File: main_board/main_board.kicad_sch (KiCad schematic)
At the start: 9 parts, among them J1 Bus_ISA_8bit, J2 IDE_44pin, J3 SIMM_30pin, J4 Keyboard, J5 Mouse, J6 5V_in, U1 M6117D, U2 SST39SF040

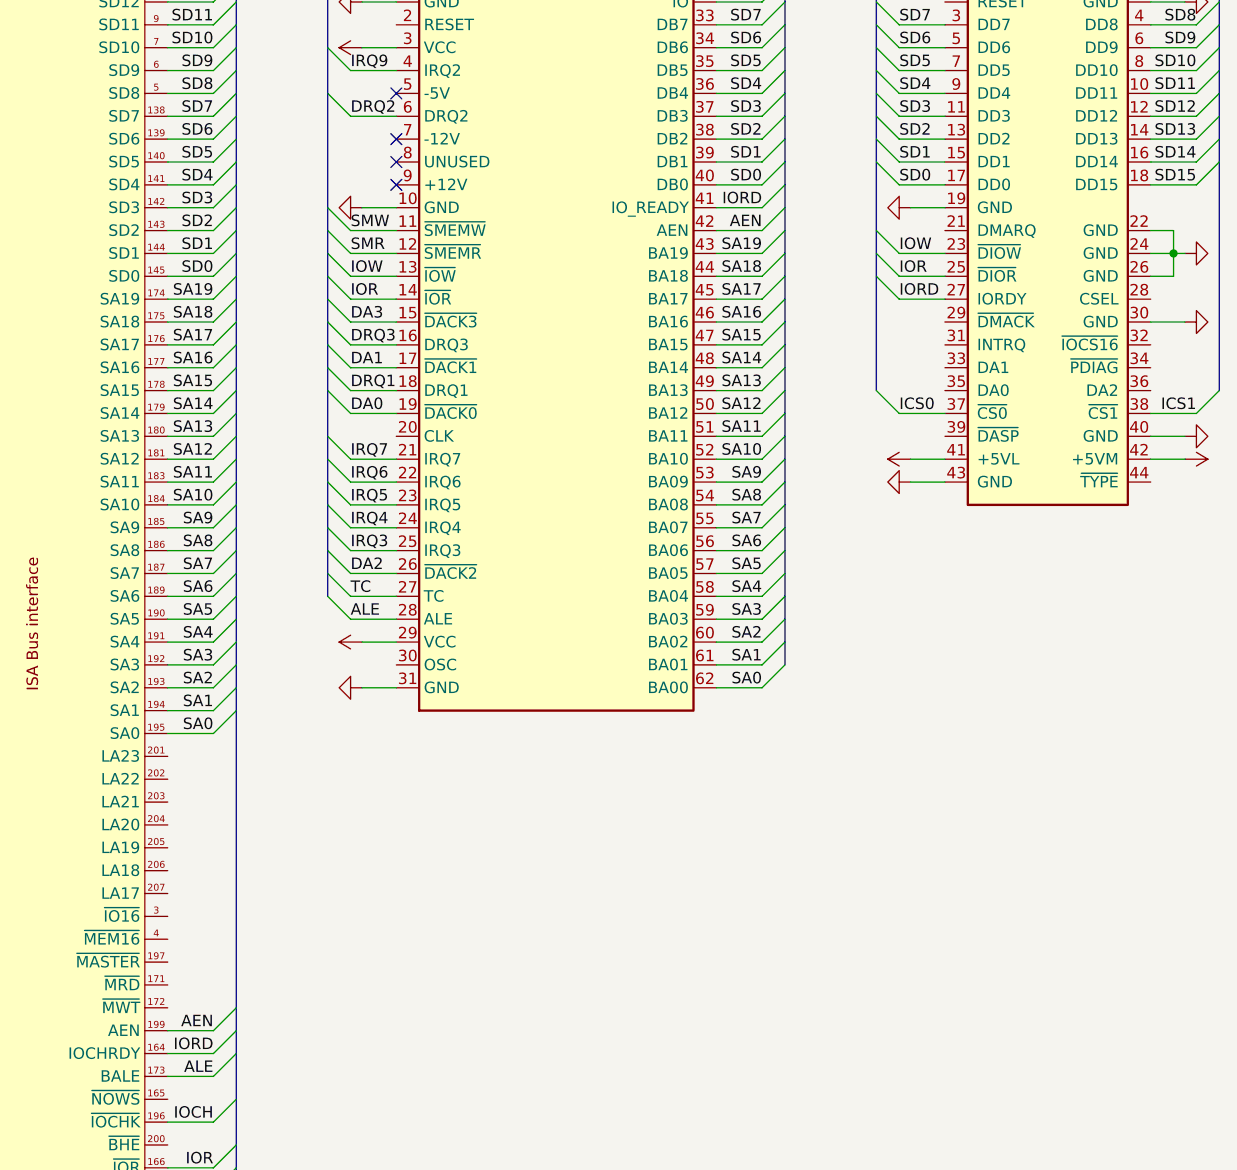
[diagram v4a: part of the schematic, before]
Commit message: connect IDE address lines to the bus
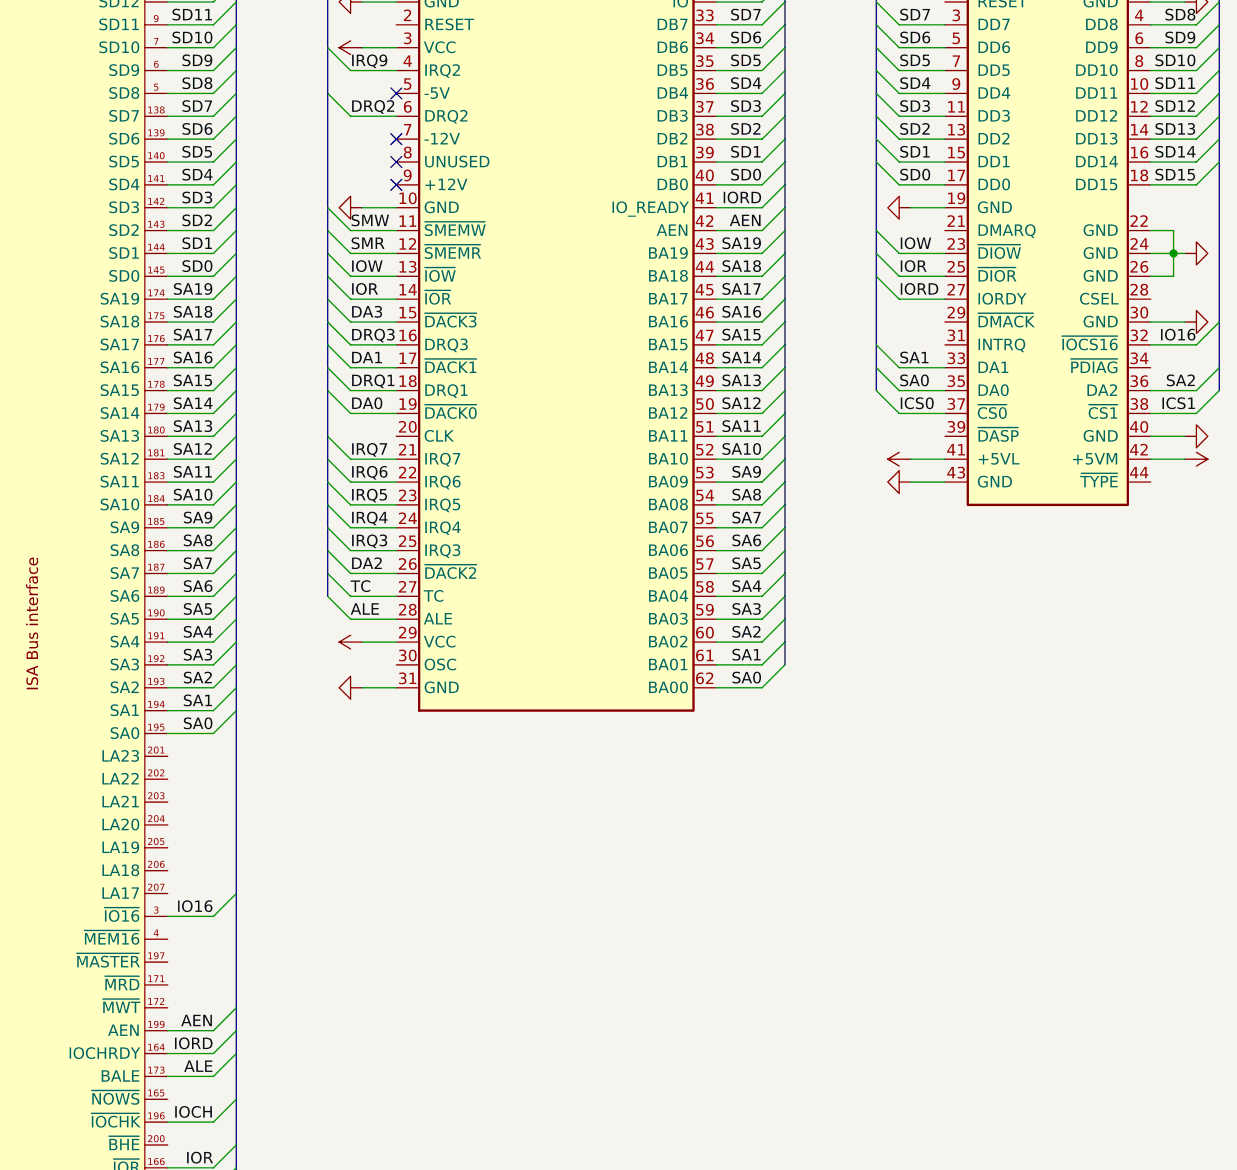
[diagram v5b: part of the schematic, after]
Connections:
- net SA0: now also J2.35 (DA0)
- net SA1: now also J2.33 (DA1)
- net SA2: now also J2.36 (DA2)
- net IO16: now reaches J2.32 (~{IOCS16})
- net IO16: now also U1.3 (~{IO16})
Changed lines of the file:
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@@
 	)
 	(bus_entry
+		(at 279.4 85.09)
+		(size 2.54 -2.54)
+		(stroke
+			(width 0)
+			(type default)
+		)
+	)
+	(bus_entry
 		(at 53.34 199.39)
 		(size 2.54 -2.54)
@@
 	)
 	(bus_entry
+		(at 246.38 90.17)
+		(size -2.54 -2.54)
+		(stroke
+			(width 0)
+			(type default)
+		)
+	)
+	(bus_entry
 		(at 53.34 250.19)
 		(size 2.54 -2.54)
@@
 	)
 	(bus_entry
+		(at 246.38 87.63)
+		(size -2.54 -2.54)
+		(stroke
+			(width 0)
+			(type default)
+		)
+	)
+	(bus_entry
 		(at 170.18 52.07)
 		(size 2.54 -2.54)
@@
 	)
 	(bus_entry
+		(at 279.4 90.17)
+		(size 2.54 -2.54)
+		(stroke
+			(width 0)
+			(type default)
+		)
+	)
+	(bus_entry
 		(at 170.18 87.63)
 		(size 2.54 -2.54)
@@
 	)
 	(bus_entry
+		(at 170.18 148.59)
+		(size 2.54 -2.54)
+		(stroke
+			(width 0)
+			(type default)
+		)
+	)
+	(bus_entry
 		(at 172.72 252.73)
 		(size -2.54 2.54)
@@
 	(bus
 		(pts
-			(xy 172.72 125.73) (xy 172.72 158.75)
+			(xy 172.72 125.73) (xy 172.72 146.05)
 		)
 		(stroke
@@
 		)
 	)
+	(bus
+		(pts
+			(xy 281.94 82.55) (xy 281.94 87.63)
+		)
+		(stroke
+			(width 0)
+			(type default)
+		)
+	)
 	(wire
 		(pts
@@
 	(wire
 		(pts
+			(xy 165.1 148.59) (xy 170.18 148.59)
+		)
+		(stroke
+			(width 0)
+			(type default)
+		)
+	)
+	(wire
+		(pts
 			(xy 165.1 57.15) (xy 170.18 57.15)
 		)
@@
 		)
 	)
+	(bus
+		(pts
+			(xy 243.84 85.09) (xy 243.84 77.47)
+		)
+		(stroke
+			(width 0)
+			(type default)
+		)
+	)
 	(wire
 		(pts
@@
 	(wire
 		(pts
+			(xy 274.32 85.09) (xy 279.4 85.09)
+		)
+		(stroke
+			(width 0)
+			(type default)
+		)
+	)
+	(wire
+		(pts
 			(xy 165.1 77.47) (xy 170.18 77.47)
 		)
@@
 		)
 	)
+	(bus
+		(pts
+			(xy 243.84 87.63) (xy 243.84 85.09)
+		)
+		(stroke
+			(width 0)
+			(type default)
+		)
+	)
 	(wire
 		(pts
@@
 		)
 	)
+	(wire
+		(pts
+			(xy 251.46 87.63) (xy 246.38 87.63)
+		)
+		(stroke
+			(width 0)
+			(type default)
+		)
+	)
 	(bus
 		(pts
@@
 	(bus
 		(pts
-			(xy 243.84 90.17) (xy 243.84 77.47)
+			(xy 243.84 90.17) (xy 243.84 87.63)
 		)
 		(stroke
@@
 	(wire
 		(pts
+			(xy 274.32 90.17) (xy 279.4 90.17)
+		)
+		(stroke
+			(width 0)
+			(type default)
+		)
+	)
+	(wire
+		(pts
 			(xy 165.1 110.49) (xy 170.18 110.49)
 		)
@@
 	(bus
 		(pts
-			(xy 281.94 64.77) (xy 281.94 90.17)
+			(xy 281.94 64.77) (xy 281.94 82.55)
 		)
 		(stroke
@@
 		)
 	)
+	(bus
+		(pts
+			(xy 281.94 87.63) (xy 281.94 90.17)
+		)
+		(stroke
+			(width 0)
+			(type default)
+		)
+	)
 	(wire
 		(pts
@@
 	(wire
 		(pts
+			(xy 251.46 90.17) (xy 246.38 90.17)
+		)
+		(stroke
+			(width 0)
+			(type default)
+		)
+	)
+	(wire
+		(pts
 			(xy 165.1 118.11) (xy 170.18 118.11)
 		)
@@
 	(bus
 		(pts
+			(xy 172.72 146.05) (xy 172.72 158.75)
+		)
+		(stroke
+			(width 0)
+			(type default)
+		)
+	)
+	(bus
+		(pts
 			(xy 55.88 201.93) (xy 55.88 196.85)
 		)
@@
 		)
 	)
+	(label "SA2"
+		(at 279.4 90.17 180)
+		(fields_autoplaced yes)
+		(effects
+			(font
+				(size 1.27 1.27)
+			)
+			(justify right bottom)
+		)
+	)
 	(label "SA5"
 		(at 231.14 110.49 180)
@@
 		)
 	)
+	(label "IO16"
+		(at 170.18 148.59 180)
+		(fields_autoplaced yes)
+		(effects
+			(font
+				(size 1.27 1.27)
+			)
+			(justify right bottom)
+		)
+	)
 	(label "RAS0"
 		(at 53.34 199.39 180)
@@
 		)
 	)
+	(label "SA0"
+		(at 246.38 90.17 0)
+		(fields_autoplaced yes)
+		(effects
+			(font
+				(size 1.27 1.27)
+			)
+			(justify left bottom)
+		)
+	)
 	(label "SD5"
 		(at 231.14 54.61 180)
@@
 		)
 	)
+	(label "IO16"
+		(at 279.4 85.09 180)
+		(fields_autoplaced yes)
+		(effects
+			(font
+				(size 1.27 1.27)
+			)
+			(justify right bottom)
+		)
+	)
+	(label "SA1"
+		(at 246.38 87.63 0)
+		(fields_autoplaced yes)
+		(effects
+			(font
+				(size 1.27 1.27)
+			)
+			(justify left bottom)
+		)
+	)
